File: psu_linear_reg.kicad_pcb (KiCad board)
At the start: 2 copper layers, 100 x 40 mm, 20 parts, among them J1 Conn_Coaxial_Power, J2 Conn_Coaxial_Power, J3 Conn_01x10_Pin, J4 Conn_01x10_Pin, J5 Conn_01x10_Pin, J6 Conn_01x10_Pin, J7 Conn_01x05, J8 Conn_01x02, U1 L7805, U2 L7905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

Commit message: Added reverse polarity protection
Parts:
- added Q1: Si4542DY, Package_SO:SOIC-8_3.9x4.9mm_P1.27mm, F.Cu at (77.0, 132.6)
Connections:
- J1 pad 1: VCC -> Net-(J1-In)
- J2 pad 1: VEE -> Net-(J2-In)
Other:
- board text added: "J Roth, M Tao, Mueller Group, UC Berkeley rev v1.2: 1-6-25"
- board text removed: "J Roth, Mueller Group, UC Berkeley"

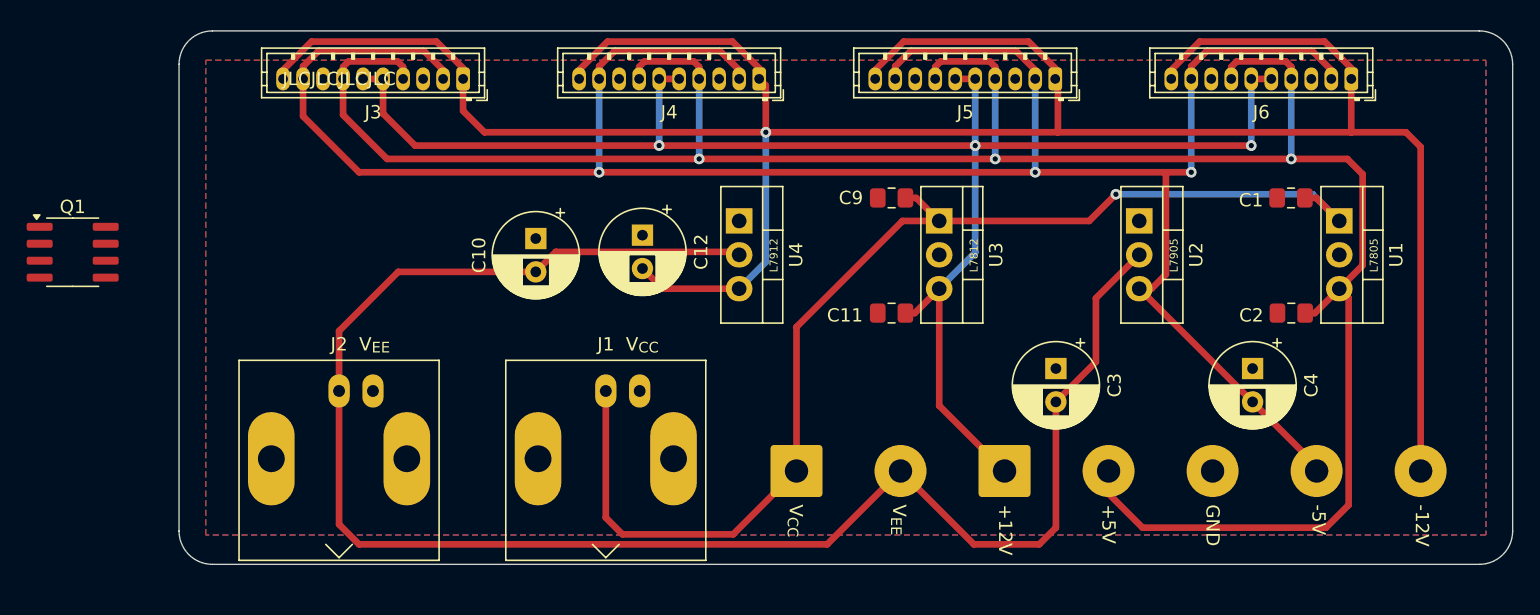
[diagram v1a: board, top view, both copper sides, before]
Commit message: Added reverse polarity protection. PCB ready for ordering
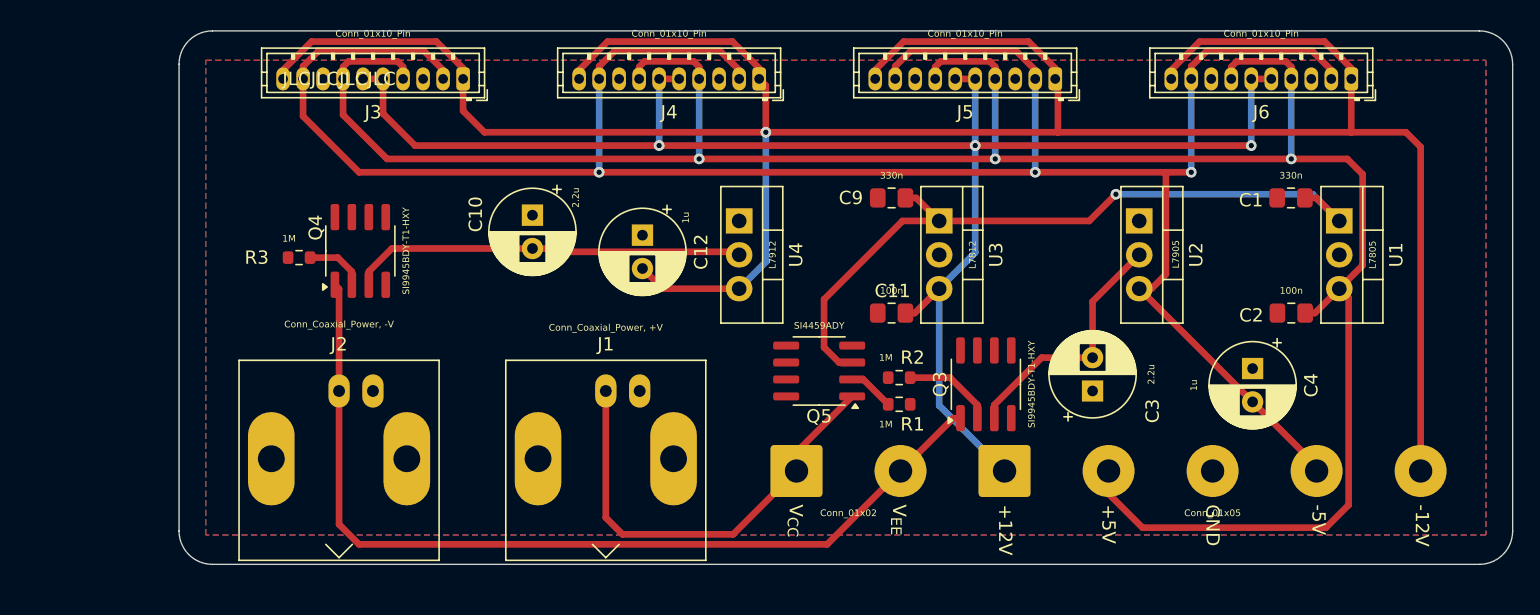
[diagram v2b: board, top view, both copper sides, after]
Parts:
- removed Q1: Si4542DY, Package_SO:SOIC-8_3.9x4.9mm_P1.27mm
- added Q3: SI9945BDY-T1-HXY, Package_SO:SOP-8_3.76x4.96mm_P1.27mm, F.Cu at (145.5, 142.5)
- added Q4: SI9945BDY-T1-HXY, Package_SO:SOP-8_3.76x4.96mm_P1.27mm, F.Cu at (98.6, 132.5)
- added Q5: SI4459ADY, Package_SO:SOIC-8_3.9x4.9mm_P1.27mm, F.Cu at (133.0, 141.5)
- added R1: 1M, Resistor_SMD:R_0603_1608Metric, F.Cu at (139.0, 144.0)
- added R2: 1M, Resistor_SMD:R_0603_1608Metric, F.Cu at (139.0, 142.0)
- added R3: 1M, Resistor_SMD:R_0603_1608Metric, F.Cu at (94.0, 133.0)
- J1: value Conn_Coaxial_Power -> Conn_Coaxial_Power, +V
- J2: value Conn_Coaxial_Power -> Conn_Coaxial_Power, -V
- moved C3 3.22 mm to (153.5, 143.0), turned to 90 degrees
- moved C10 1.77 mm to (111.5, 129.8)
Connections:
- C1 pad 1: VCC -> Net-(Q5-S)
- C10 pad 2: VEE -> Net-(Q4-S)
- C3 pad 2: VEE -> Net-(Q3-S)
- C9 pad 1: VCC -> Net-(Q5-S)
- J1 pad 1: Net-(J1-In) -> VCC
- J2 pad 1: Net-(J2-In) -> VEE
- U1 pad 1: VCC -> Net-(Q5-S)
- U2 pad 2: VEE -> Net-(Q3-S)
- U3 pad 1: VCC -> Net-(Q5-S)
- U4 pad 2: VEE -> Net-(Q4-S)
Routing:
- net VEE: track 129.9 -> 69.2 mm
- net VCC: track 89.3 -> 33.6 mm, vias 1 -> 0
- net Net-(Q5-S): track 0.00 -> 55.4 mm, vias 0 -> 1
- net Net-(Q4-S): track 0.00 -> 30.0 mm
- net Net-(Q3-S): track 0.00 -> 19.0 mm
- net Net-(Q3-G): track 0.00 -> 6.88 mm
- net Net-(Q4-G): track 0.00 -> 4.56 mm
- net Net-(Q5-G): track 0.00 -> 3.47 mm
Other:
- board text removed: "L7805"
- board text removed: "L7812"
- board text removed: "L7905"
- board text removed: "L7912"
